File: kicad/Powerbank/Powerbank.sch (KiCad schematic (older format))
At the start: 0 parts

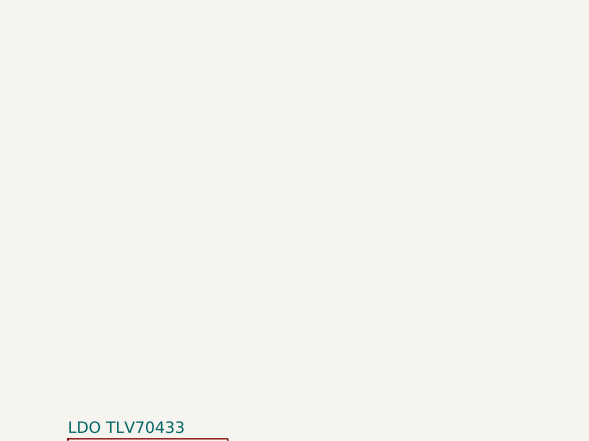
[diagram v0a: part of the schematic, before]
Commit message: Battery charger completed according to reference guide
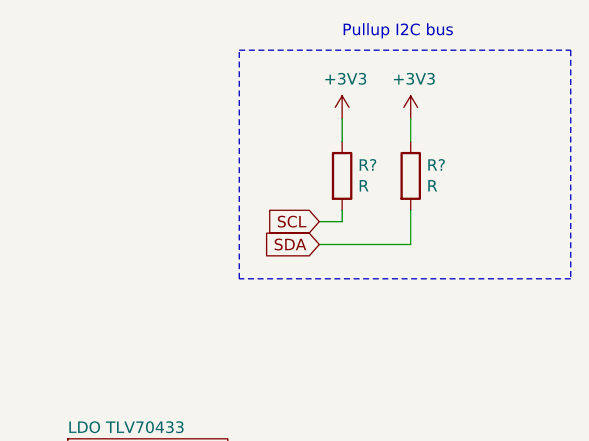
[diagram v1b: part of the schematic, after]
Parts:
- added R? (x2): R, symbol Device:R
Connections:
- new net +3V3: R?.1, R?.1
- new net SCL: R?.2
- new net SDA: R?.2
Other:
- note added: "Pullup I2C bus"
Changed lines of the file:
@@
 F1 "Battery.sch" 50
 $EndSheet
+Text GLabel 8900 2250 0    50   Input ~ 0
+SCL
+Text GLabel 8900 2350 0    50   Input ~ 0
+SDA
+$Comp
+L Device:R R?
+U 1 1 5E3AB7DA
+P 9000 2050
+F 0 "R?" H 9070 2096 50  0000 L CNN
+F 1 "R" H 9070 2005 50  0000 L CNN
+F 2 "" V 8930 2050 50  0001 C CNN
+F 3 "~" H 9000 2050 50  0001 C CNN
+	1    9000 2050
+	1    0    0    -1
+$EndComp
+$Comp
+L Device:R R?
+U 1 1 5E3AC18F
+P 9300 2050
+F 0 "R?" H 9370 2096 50  0000 L CNN
+F 1 "R" H 9370 2005 50  0000 L CNN
+F 2 "" V 9230 2050 50  0001 C CNN
+F 3 "~" H 9300 2050 50  0001 C CNN
+	1    9300 2050
+	1    0    0    -1
+$EndComp
+Wire Wire Line
+	9000 2200 9000 2250
+Wire Wire Line
+	9000 2250 8900 2250
+Wire Wire Line
+	9300 2350 9300 2200
+Wire Wire Line
+	8900 2350 9300 2350
+$Comp
+L power:+3V3 #PWR?
+U 1 1 5E3AC810
+P 9000 1800
+F 0 "#PWR?" H 9000 1650 50  0001 C CNN
+F 1 "+3V3" H 9015 1973 50  0000 C CNN
+F 2 "" H 9000 1800 50  0001 C CNN
+F 3 "" H 9000 1800 50  0001 C CNN
+	1    9000 1800
+	1    0    0    -1
+$EndComp
+$Comp
+L power:+3V3 #PWR?
+U 1 1 5E3AD0F6
+P 9300 1800
+F 0 "#PWR?" H 9300 1650 50  0001 C CNN
+F 1 "+3V3" H 9315 1973 50  0000 C CNN
+F 2 "" H 9300 1800 50  0001 C CNN
+F 3 "" H 9300 1800 50  0001 C CNN
+	1    9300 1800
+	1    0    0    -1
+$EndComp
+Wire Wire Line
+	9300 1800 9300 1900
+Wire Wire Line
+	9000 1800 9000 1900
+Wire Notes Line
+	8550 1500 10000 1500
+Wire Notes Line
+	10000 1500 10000 2500
+Wire Notes Line
+	10000 2500 8550 2500
+Wire Notes Line
+	8550 2500 8550 1500
+Text Notes 9000 1450 0    50   ~ 0
+Pullup I2C bus
 $EndSCHEMATC

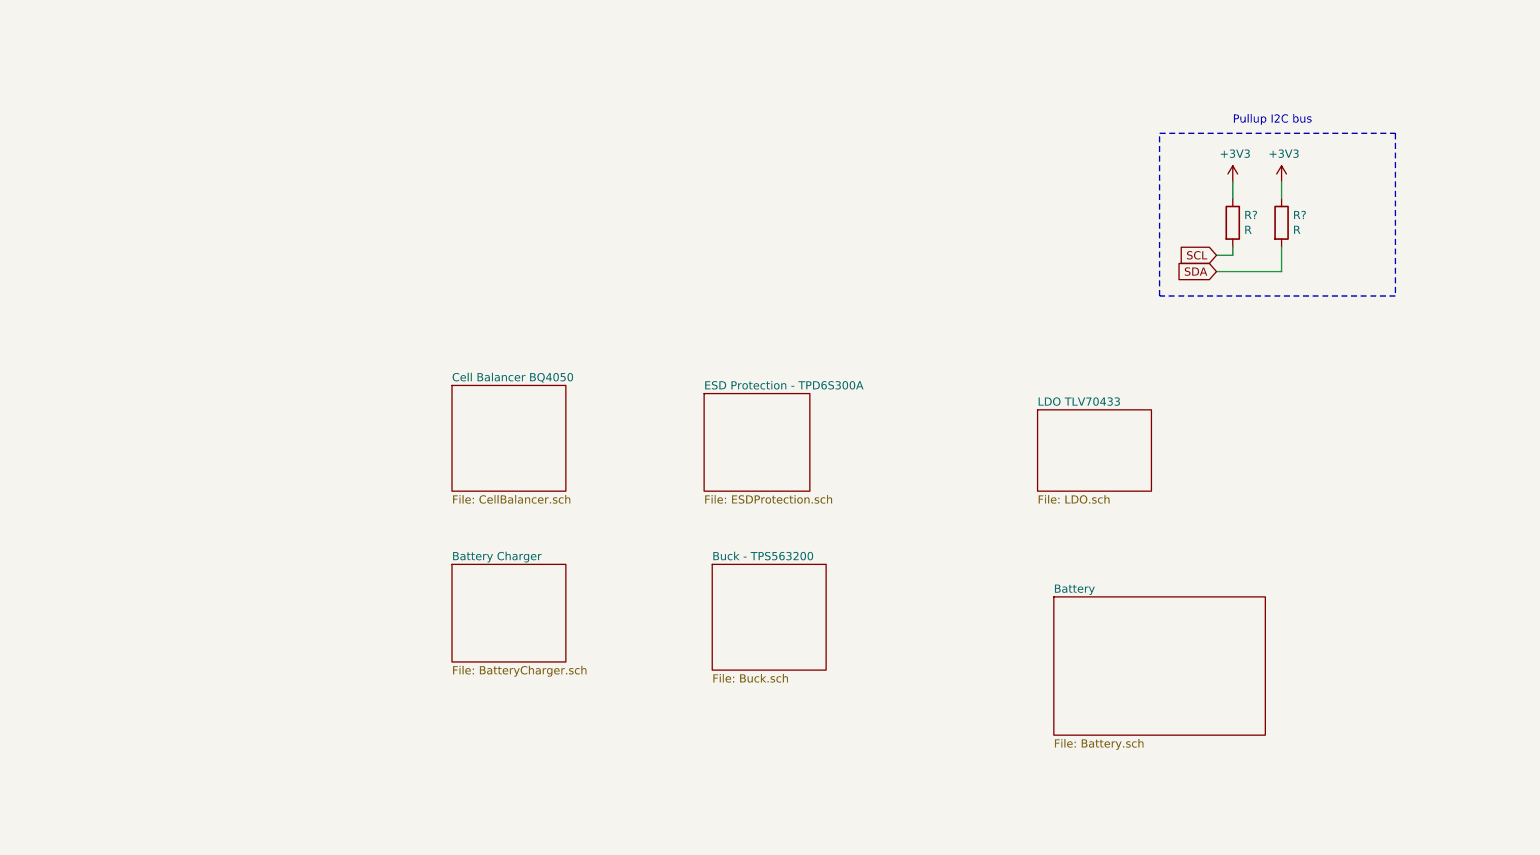
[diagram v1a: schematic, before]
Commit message: Added PD Controller according to reference design
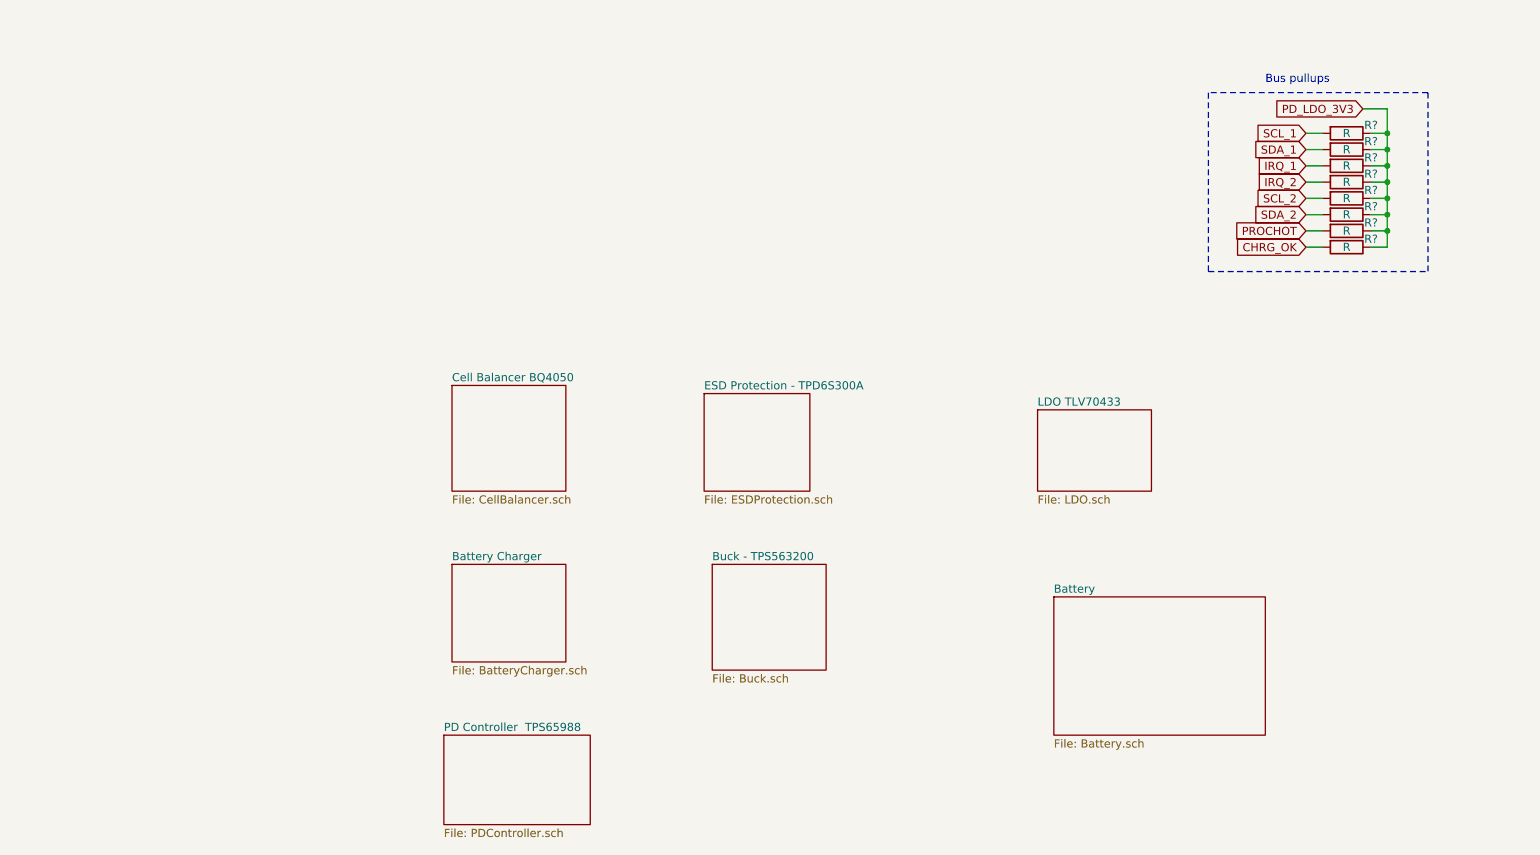
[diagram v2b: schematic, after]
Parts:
- removed R?: R, symbol Device:R
- added R? (x7): R, symbol Device:R
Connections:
- net +3V3 renamed PD_LDO_3V3
- net PD_LDO_3V3: now also R?.1, R?.1, R?.1, R?.1, R?.1, R?.1, R?.1
- net SCL renamed SCL_1
- new net CHRG_OK: R?.2
- new net IRQ_1: R?.2
- new net IRQ_2: R?.2
- new net PROCHOT: R?.2
- new net SCL_2: R?.2
- new net SDA_1: R?.2
- new net SDA_2: R?.2
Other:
- note added: "Bus pullups"
- note removed: "Pullup I2C bus"
- moved on the sheet: R?
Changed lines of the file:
@@
 $Descr A4 11693 8268
 encoding utf-8
-Sheet 1 7
+Sheet 1 8
 Title ""
 Date ""
@@
 F1 "Battery.sch" 50
 $EndSheet
-Text GLabel 8900 2250 0    50   Input ~ 0
-SCL
-Text GLabel 8900 2350 0    50   Input ~ 0
-SDA
+Text GLabel 9450 1500 0    50   Input ~ 0
+SCL_1
+Text GLabel 9450 1600 0    50   Input ~ 0
+SDA_1
 $Comp
 L Device:R R?
 U 1 1 5E3AB7DA
-P 9000 2050
-F 0 "R?" H 9070 2096 50  0000 L CNN
-F 1 "R" H 9070 2005 50  0000 L CNN
-F 2 "" V 8930 2050 50  0001 C CNN
-F 3 "~" H 9000 2050 50  0001 C CNN
-	1    9000 2050
-	1    0    0    -1
-$EndComp
-$Comp
-L Device:R R?
-U 1 1 5E3AC18F
-P 9300 2050
-F 0 "R?" H 9370 2096 50  0000 L CNN
-F 1 "R" H 9370 2005 50  0000 L CNN
-F 2 "" V 9230 2050 50  0001 C CNN
-F 3 "~" H 9300 2050 50  0001 C CNN
-	1    9300 2050
-	1    0    0    -1
-$EndComp
-Wire Wire Line
-	9000 2200 9000 2250
-Wire Wire Line
-	9000 2250 8900 2250
-Wire Wire Line
-	9300 2350 9300 2200
-Wire Wire Line
-	8900 2350 9300 2350
-$Comp
-L power:+3V3 #PWR?
-U 1 1 5E3AC810
-P 9000 1800
-F 0 "#PWR?" H 9000 1650 50  0001 C CNN
-F 1 "+3V3" H 9015 1973 50  0000 C CNN
-F 2 "" H 9000 1800 50  0001 C CNN
-F 3 "" H 9000 1800 50  0001 C CNN
-	1    9000 1800
-	1    0    0    -1
-$EndComp
-$Comp
-L power:+3V3 #PWR?
-U 1 1 5E3AD0F6
-P 9300 1800
-F 0 "#PWR?" H 9300 1650 50  0001 C CNN
-F 1 "+3V3" H 9315 1973 50  0000 C CNN
-F 2 "" H 9300 1800 50  0001 C CNN
-F 3 "" H 9300 1800 50  0001 C CNN
-	1    9300 1800
-	1    0    0    -1
-$EndComp
-Wire Wire Line
-	9300 1800 9300 1900
-Wire Wire Line
-	9000 1800 9000 1900
-Wire Notes Line
-	8550 1500 10000 1500
-Wire Notes Line
-	10000 1500 10000 2500
-Wire Notes Line
-	10000 2500 8550 2500
-Wire Notes Line
-	8550 2500 8550 1500
-Text Notes 9000 1450 0    50   ~ 0
-Pullup I2C bus
+P 9700 1500
+F 0 "R?" V 9650 1650 50  0000 C CNN
+F 1 "R" V 9700 1500 50  0000 C CNN
+F 2 "" V 9630 1500 50  0001 C CNN
+F 3 "~" H 9700 1500 50  0001 C CNN
+	1    9700 1500
+	0    1    1    0
+$EndComp
+Text Notes 9200 1200 0    50   ~ 0
+Bus pullups
+$Sheet
+S 4150 5200 900  550
+U 5E7BFD38
+F0 "PD Controller  TPS65988" 50
+F1 "PDController.sch" 50
+$EndSheet
+$Comp
+L Device:R R?
+U 1 1 5E7D5CC8
+P 9700 1600
+F 0 "R?" V 9650 1750 50  0000 C CNN
+F 1 "R" V 9700 1600 50  0000 C CNN
+F 2 "" V 9630 1600 50  0001 C CNN
+F 3 "~" H 9700 1600 50  0001 C CNN
+	1    9700 1600
+	0    1    1    0
+$EndComp
+$Comp
+L Device:R R?
+U 1 1 5E7D5F09
+P 9700 1700
+F 0 "R?" V 9650 1850 50  0000 C CNN
+F 1 "R" V 9700 1700 50  0000 C CNN
+F 2 "" V 9630 1700 50  0001 C CNN
+F 3 "~" H 9700 1700 50  0001 C CNN
+	1    9700 1700
+	0    1    1    0
+$EndComp
+$Comp
+L Device:R R?
+U 1 1 5E7D608C
+P 9700 1800
+F 0 "R?" V 9650 1950 50  0000 C CNN
+F 1 "R" V 9700 1800 50  0000 C CNN
+F 2 "" V 9630 1800 50  0001 C CNN
+F 3 "~" H 9700 1800 50  0001 C CNN
+	1    9700 1800
+	0    1    1    0
+$EndComp
+$Comp
+L Device:R R?
+U 1 1 5E7D632E
+P 9700 1900
+F 0 "R?" V 9650 2050 50  0000 C CNN
+F 1 "R" V 9700 1900 50  0000 C CNN
+F 2 "" V 9630 1900 50  0001 C CNN
+F 3 "~" H 9700 1900 50  0001 C CNN
+	1    9700 1900
+	0    1    1    0
+$EndComp
+$Comp
+L Device:R R?
+U 1 1 5E7D678C
+P 9700 2000
+F 0 "R?" V 9650 2150 50  0000 C CNN
+F 1 "R" V 9700 2000 50  0000 C CNN
+F 2 "" V 9630 2000 50  0001 C CNN
+F 3 "~" H 9700 2000 50  0001 C CNN
+	1    9700 2000
+	0    1    1    0
+$EndComp
+$Comp
+L Device:R R?
+U 1 1 5E7D699A
+P 9700 2100
+F 0 "R?" V 9650 2250 50  0000 C CNN
+F 1 "R" V 9700 2100 50  0000 C CNN
+F 2 "" V 9630 2100 50  0001 C CNN
+F 3 "~" H 9700 2100 50  0001 C CNN
+	1    9700 2100
+	0    1    1    0
+$EndComp
+$Comp
+L Device:R R?
+U 1 1 5E7D6C41
+P 9700 2200
+F 0 "R?" V 9650 2350 50  0000 C CNN
+F 1 "R" V 9700 2200 50  0000 C CNN
+F 2 "" V 9630 2200 50  0001 C CNN
+F 3 "~" H 9700 2200 50  0001 C CNN
+	1    9700 2200
+	0    1    1    0
+$EndComp
+Wire Wire Line
+	9850 2200 9950 2200
+Wire Wire Line
+	9950 2200 9950 2100
+Wire Wire Line
+	9950 1500 9850 1500
+Wire Wire Line
+	9850 1600 9950 1600
+Connection ~ 9950 1600
+Wire Wire Line
+	9950 1600 9950 1500
+Wire Wire Line
+	9850 1700 9950 1700
+Connection ~ 9950 1700
+Wire Wire Line
+	9950 1700 9950 1600
+Wire Wire Line
+	9850 1800 9950 1800
+Connection ~ 9950 1800
+Wire Wire Line
+	9950 1800 9950 1700
+Wire Wire Line
+	9850 1900 9950 1900
+Connection ~ 9950 1900
+Wire Wire Line
+	9950 1900 9950 1800
+Wire Wire Line
+	9850 2000 9950 2000
+Connection ~ 9950 2000
+Wire Wire Line
+	9950 2000 9950 1900
+Wire Wire Line
+	9850 2100 9950 2100
+Connection ~ 9950 2100
+Wire Wire Line
+	9950 2100 9950 2000
+Text GLabel 9800 1350 0    50   Input ~ 0
+PD_LDO_3V3
+Text GLabel 9450 1700 0    50   Input ~ 0
+IRQ_1
+Text GLabel 9450 1800 0    50   Input ~ 0
+IRQ_2
+Text GLabel 9450 1900 0    50   Input ~ 0
+SCL_2
+Text GLabel 9450 2000 0    50   Input ~ 0
+SDA_2
+Text GLabel 9450 2100 0    50   Input ~ 0
+PROCHOT
+Text GLabel 9450 2200 0    50   Input ~ 0
+CHRG_OK
+Wire Wire Line
+	9450 2200 9550 2200
+Wire Wire Line
+	9550 2100 9450 2100
+Wire Wire Line
+	9450 2000 9550 2000
+Wire Wire Line
+	9550 1900 9450 1900
+Wire Wire Line
+	9450 1800 9550 1800
+Wire Wire Line
+	9550 1700 9450 1700
+Wire Wire Line
+	9450 1600 9550 1600
+Wire Wire Line
+	9550 1500 9450 1500
+Wire Wire Line
+	9950 1350 9950 1500
+Wire Wire Line
+	9800 1350 9950 1350
+Connection ~ 9950 1500
+Wire Notes Line
+	10200 1250 10200 2350
+Wire Notes Line
+	10200 1250 8850 1250
+Wire Notes Line
+	8850 1250 8850 2350
+Wire Notes Line
+	8850 2350 10200 2350
 $EndSCHEMATC

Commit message: Moved LDO to Buck sheet and started check of components
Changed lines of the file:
@@
 $Descr A4 11693 8268
 encoding utf-8
-Sheet 1 8
+Sheet 1 7
 Title ""
 Date ""
@@
 $EndSheet
 $Sheet
-S 7800 3200 700  500
-U 5E0D16A0
-F0 "LDO TLV70433" 50
-F1 "LDO.sch" 50
-$EndSheet
-$Sheet

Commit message: Double checked schematic towards reference design
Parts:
- R? (x6): value R -> 3.83k
- R? (x2): value R -> 10k
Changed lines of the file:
@@
 P 9700 1500
 F 0 "R?" V 9650 1650 50  0000 C CNN
-F 1 "R" V 9700 1500 50  0000 C CNN
+F 1 "3.83k" V 9700 1500 50  0000 C CNN
 F 2 "" V 9630 1500 50  0001 C CNN
 F 3 "~" H 9700 1500 50  0001 C CNN
@@
 P 9700 1600
 F 0 "R?" V 9650 1750 50  0000 C CNN
-F 1 "R" V 9700 1600 50  0000 C CNN
+F 1 "3.83k" V 9700 1600 50  0000 C CNN
 F 2 "" V 9630 1600 50  0001 C CNN
 F 3 "~" H 9700 1600 50  0001 C CNN
@@
 P 9700 1700
 F 0 "R?" V 9650 1850 50  0000 C CNN
-F 1 "R" V 9700 1700 50  0000 C CNN
+F 1 "10k" V 9700 1700 50  0000 C CNN
 F 2 "" V 9630 1700 50  0001 C CNN
 F 3 "~" H 9700 1700 50  0001 C CNN
@@
 P 9700 1800
 F 0 "R?" V 9650 1950 50  0000 C CNN
-F 1 "R" V 9700 1800 50  0000 C CNN
+F 1 "10k" V 9700 1800 50  0000 C CNN
 F 2 "" V 9630 1800 50  0001 C CNN
 F 3 "~" H 9700 1800 50  0001 C CNN
@@
 P 9700 1900
 F 0 "R?" V 9650 2050 50  0000 C CNN
-F 1 "R" V 9700 1900 50  0000 C CNN
+F 1 "3.83k" V 9700 1900 50  0000 C CNN
 F 2 "" V 9630 1900 50  0001 C CNN
 F 3 "~" H 9700 1900 50  0001 C CNN
@@
 P 9700 2000
 F 0 "R?" V 9650 2150 50  0000 C CNN
-F 1 "R" V 9700 2000 50  0000 C CNN
+F 1 "3.83k" V 9700 2000 50  0000 C CNN
 F 2 "" V 9630 2000 50  0001 C CNN
 F 3 "~" H 9700 2000 50  0001 C CNN
@@
 P 9700 2100
 F 0 "R?" V 9650 2250 50  0000 C CNN
-F 1 "R" V 9700 2100 50  0000 C CNN
+F 1 "3.83k" V 9700 2100 50  0000 C CNN
 F 2 "" V 9630 2100 50  0001 C CNN
 F 3 "~" H 9700 2100 50  0001 C CNN
@@
 P 9700 2200
 F 0 "R?" V 9650 2350 50  0000 C CNN
-F 1 "R" V 9700 2200 50  0000 C CNN
+F 1 "3.83k" V 9700 2200 50  0000 C CNN
 F 2 "" V 9630 2200 50  0001 C CNN
 F 3 "~" H 9700 2200 50  0001 C CNN

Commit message: Updated for PCB
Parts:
- R1, R2, R3, R4, R5, R6, R7, R8: renamed from R?; footprint (none) -> Resistor_SMD:R_0603_1608Metric
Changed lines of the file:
@@
 EESchema Schematic File Version 4
+LIBS:Powerbank-cache
 EELAYER 30 0
 EELAYER END
@@
 SDA_1
 $Comp
-L Device:R R?
+L Device:R R1
 U 1 1 5E3AB7DA
 P 9700 1500
-F 0 "R?" V 9650 1650 50  0000 C CNN
+F 0 "R1" V 9650 1650 50  0000 C CNN
 F 1 "3.83k" V 9700 1500 50  0000 C CNN
-F 2 "" V 9630 1500 50  0001 C CNN
+F 2 "Resistor_SMD:R_0603_1608Metric" V 9630 1500 50  0001 C CNN
 F 3 "~" H 9700 1500 50  0001 C CNN
 	1    9700 1500
@@
 $EndSheet
 $Comp
-L Device:R R?
+L Device:R R2
 U 1 1 5E7D5CC8
 P 9700 1600
-F 0 "R?" V 9650 1750 50  0000 C CNN
+F 0 "R2" V 9650 1750 50  0000 C CNN
 F 1 "3.83k" V 9700 1600 50  0000 C CNN
-F 2 "" V 9630 1600 50  0001 C CNN
+F 2 "Resistor_SMD:R_0603_1608Metric" V 9630 1600 50  0001 C CNN
 F 3 "~" H 9700 1600 50  0001 C CNN
 	1    9700 1600
@@
 $EndComp
 $Comp
-L Device:R R?
+L Device:R R3
 U 1 1 5E7D5F09
 P 9700 1700
-F 0 "R?" V 9650 1850 50  0000 C CNN
+F 0 "R3" V 9650 1850 50  0000 C CNN
 F 1 "10k" V 9700 1700 50  0000 C CNN
-F 2 "" V 9630 1700 50  0001 C CNN
+F 2 "Resistor_SMD:R_0603_1608Metric" V 9630 1700 50  0001 C CNN
 F 3 "~" H 9700 1700 50  0001 C CNN
 	1    9700 1700
@@
 $EndComp
 $Comp
-L Device:R R?
+L Device:R R4
 U 1 1 5E7D608C
 P 9700 1800
-F 0 "R?" V 9650 1950 50  0000 C CNN
+F 0 "R4" V 9650 1950 50  0000 C CNN
 F 1 "10k" V 9700 1800 50  0000 C CNN
-F 2 "" V 9630 1800 50  0001 C CNN
+F 2 "Resistor_SMD:R_0603_1608Metric" V 9630 1800 50  0001 C CNN
 F 3 "~" H 9700 1800 50  0001 C CNN
 	1    9700 1800
@@
 $EndComp
 $Comp
-L Device:R R?
+L Device:R R5
 U 1 1 5E7D632E
 P 9700 1900
-F 0 "R?" V 9650 2050 50  0000 C CNN
+F 0 "R5" V 9650 2050 50  0000 C CNN
 F 1 "3.83k" V 9700 1900 50  0000 C CNN
-F 2 "" V 9630 1900 50  0001 C CNN
+F 2 "Resistor_SMD:R_0603_1608Metric" V 9630 1900 50  0001 C CNN
 F 3 "~" H 9700 1900 50  0001 C CNN
 	1    9700 1900
@@
 $EndComp
 $Comp
-L Device:R R?
+L Device:R R6
 U 1 1 5E7D678C
 P 9700 2000
-F 0 "R?" V 9650 2150 50  0000 C CNN
+F 0 "R6" V 9650 2150 50  0000 C CNN
 F 1 "3.83k" V 9700 2000 50  0000 C CNN
-F 2 "" V 9630 2000 50  0001 C CNN
+F 2 "Resistor_SMD:R_0603_1608Metric" V 9630 2000 50  0001 C CNN
 F 3 "~" H 9700 2000 50  0001 C CNN
 	1    9700 2000
@@
 $EndComp
 $Comp
-L Device:R R?
+L Device:R R7
 U 1 1 5E7D699A
 P 9700 2100
-F 0 "R?" V 9650 2250 50  0000 C CNN
+F 0 "R7" V 9650 2250 50  0000 C CNN
 F 1 "3.83k" V 9700 2100 50  0000 C CNN
-F 2 "" V 9630 2100 50  0001 C CNN
+F 2 "Resistor_SMD:R_0603_1608Metric" V 9630 2100 50  0001 C CNN
 F 3 "~" H 9700 2100 50  0001 C CNN
 	1    9700 2100
@@
 $EndComp
 $Comp
-L Device:R R?
+L Device:R R8
 U 1 1 5E7D6C41
 P 9700 2200
-F 0 "R?" V 9650 2350 50  0000 C CNN
+F 0 "R8" V 9650 2350 50  0000 C CNN
 F 1 "3.83k" V 9700 2200 50  0000 C CNN
-F 2 "" V 9630 2200 50  0001 C CNN
+F 2 "Resistor_SMD:R_0603_1608Metric" V 9630 2200 50  0001 C CNN
 F 3 "~" H 9700 2200 50  0001 C CNN
 	1    9700 2200
